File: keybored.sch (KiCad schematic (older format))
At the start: 7 parts, among them U1 ATMEGA32U4

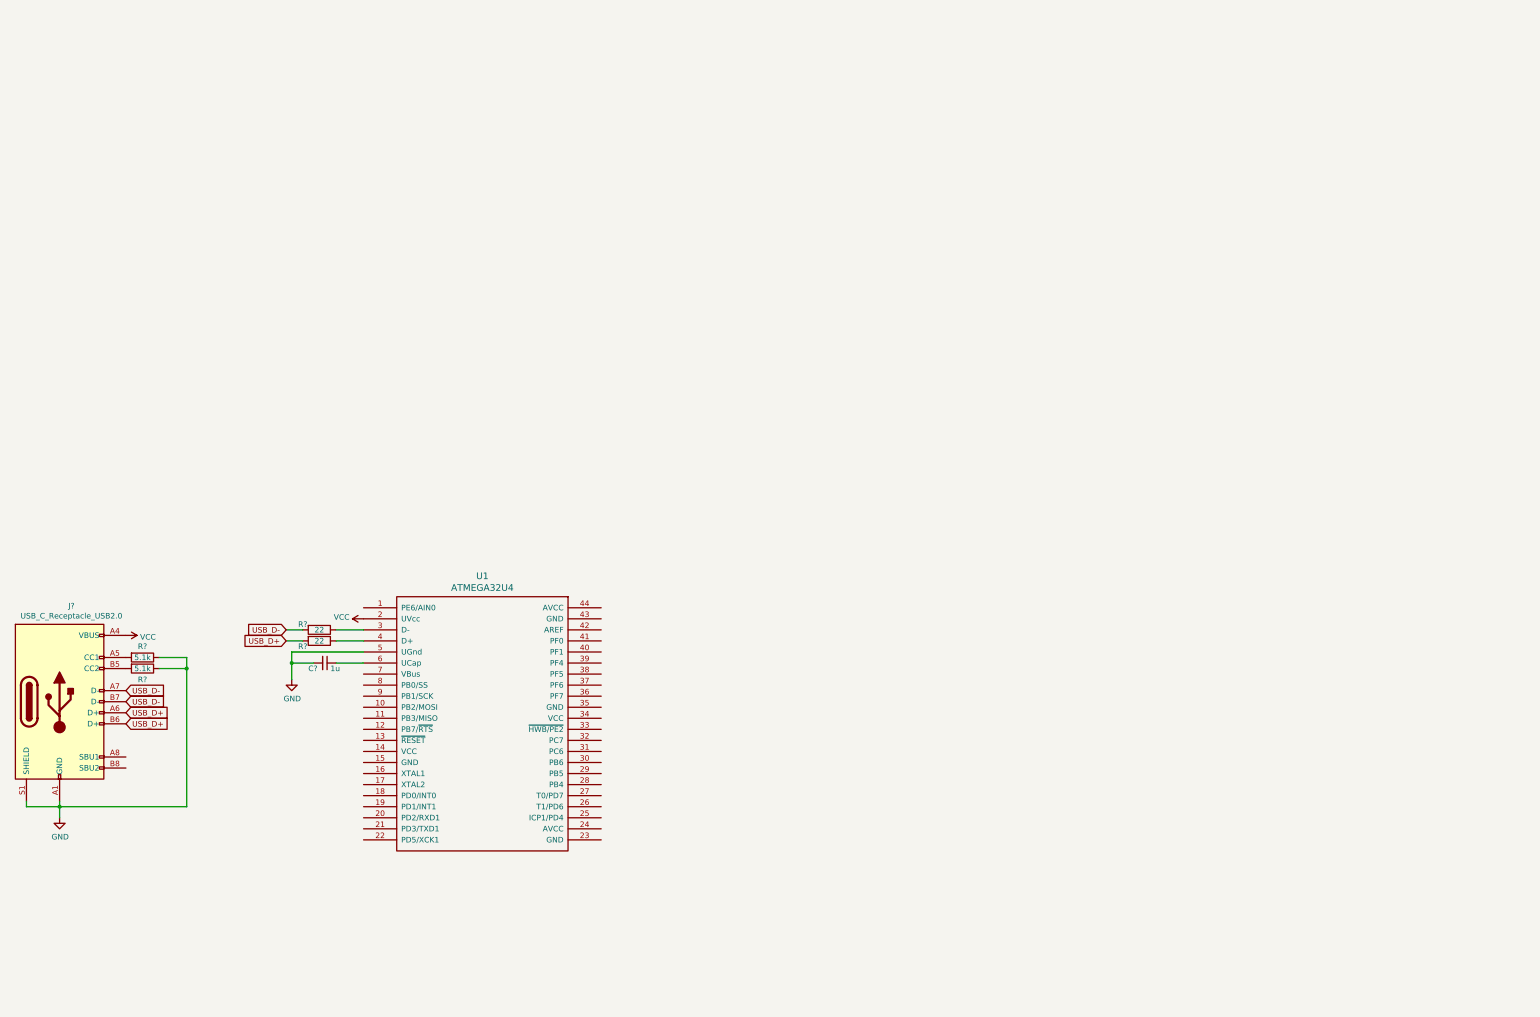
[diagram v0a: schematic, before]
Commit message: Added Schematic
- USB, reset implemented
- matrix pinouts still WIP
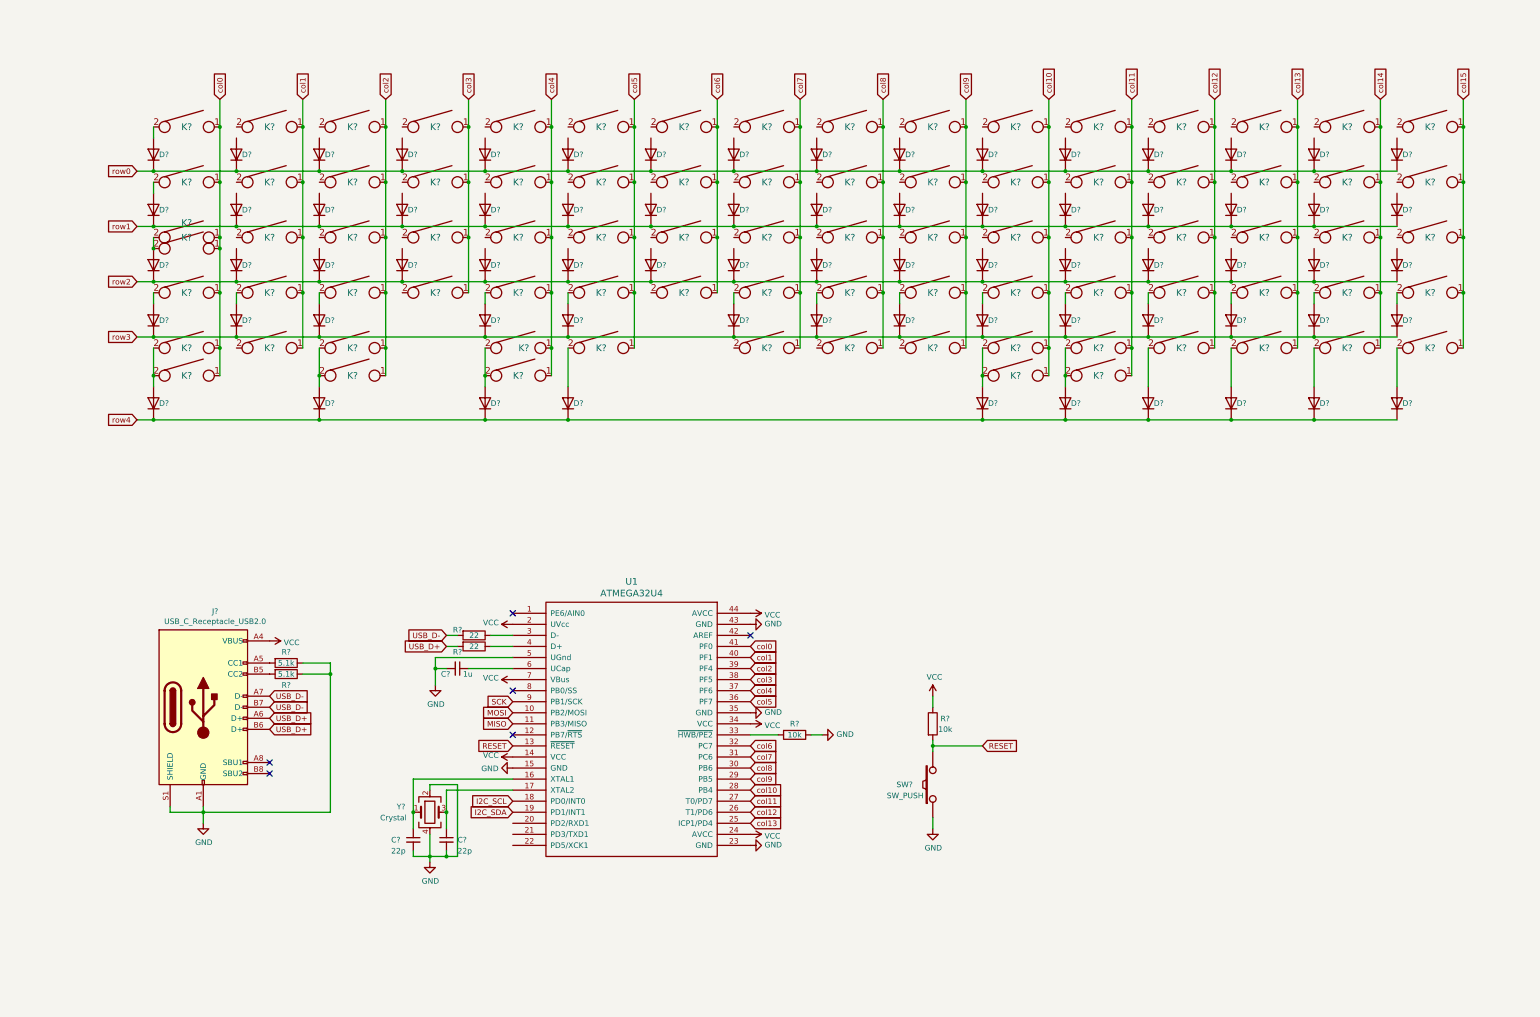
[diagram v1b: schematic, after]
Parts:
- added C? (x2): 22p, symbol Device:C_Small
- added D? (x72): D, symbol Device:D
- added K? (x84): KEYSW, symbol keyboard_parts:KEYSW
- added R? (x2): 10k, symbol Device:R
- added SW?: SW_PUSH, symbol keyboard_parts:SW_PUSH
- added Y?: Crystal, symbol Device:Crystal_GND24
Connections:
- net GND: now also U1.15 (GND), U1.23 (GND), U1.35 (GND), U1.43 (GND), C?.2, C?.2, R?.1, SW?.1, Y?.2, Y?.4
- net VCC: now also U1.14 (VCC), U1.24 (AVCC), U1.34 (VCC), U1.44 (AVCC), U1.7 (VBus), R?.1
- net MOSI: now reaches U1.10 (PB2/MOSI)
- net MISO: now reaches U1.11 (PB3/MISO)
- net RESET: now reaches U1.13 (~RESET)
- net RESET: now also R?.2, SW?.2
- net at U1.16 (XTAL1): now also C?.1, Y?.1
- net at U1.17 (XTAL2): now also C?.1, Y?.3
- net I2C_SCL: now reaches U1.18 (PD0/INT0)
- net I2C_SDA: now reaches U1.19 (PD1/INT1)
- net col13: now reaches U1.25 (ICP1/PD4)
- net col13: now also K?.1, K?.1, K?.1, K?.1, K?.1
- net col12: now reaches U1.26 (T1/PD6)
- net col12: now also K?.1, K?.1, K?.1, K?.1, K?.1
- net col11: now reaches U1.27 (T0/PD7)
- net col11: now also K?.1, K?.1, K?.1, K?.1, K?.1, K?.1
- net col10: now reaches U1.28 (PB4)
- net col10: now also K?.1, K?.1, K?.1, K?.1, K?.1, K?.1
- net col9: now reaches U1.29 (PB5)
- net col9: now also K?.1, K?.1, K?.1, K?.1, K?.1
- net col8: now reaches U1.30 (PB6)
- net col8: now also K?.1, K?.1, K?.1, K?.1, K?.1
- net col7: now reaches U1.31 (PC6)
- net col7: now also K?.1, K?.1, K?.1, K?.1, K?.1
- net col6: now reaches U1.32 (PC7)
- net col6: now also K?.1, K?.1, K?.1, K?.1
- net at U1.33 (~HWB/PE2): now also R?.2
- net col5: now reaches U1.36 (PF7)
- net col5: now also K?.1, K?.1, K?.1, K?.1, K?.1
- net col4: now reaches U1.37 (PF6)
- net col4: now also K?.1, K?.1, K?.1, K?.1, K?.1, K?.1
- net col3: now reaches U1.38 (PF5)
- net col3: now also K?.1, K?.1, K?.1, K?.1
- net col2: now reaches U1.39 (PF4)
- net col2: now also K?.1, K?.1, K?.1, K?.1, K?.1, K?.1
- net col1: now reaches U1.40 (PF1)
- net col1: now also K?.1, K?.1, K?.1, K?.1, K?.1
- net col0: now reaches U1.41 (PF0)
- net col0: now also K?.1, K?.1, K?.1, K?.1, K?.1, K?.1, K?.1
- net SCK: now reaches U1.9 (PB1/SCK)
- new net: D?.2 (A), K?.2 (x21)
- new net: D?.2 (A), K?.2, K?.2 (x6)
- new net col14: K?.1, K?.1, K?.1, K?.1, K?.1
- new net col15: K?.1, K?.1, K?.1, K?.1, K?.1
- new net row0: D?.1 (K), D?.1 (K), D?.1 (K), D?.1 (K), D?.1 (K), D?.1 (K), D?.1 (K), D?.1 (K), D?.1 (K), D?.1 (K), D?.1 (K), D?.1 (K), D?.1 (K), D?.1 (K), D?.1 (K), D?.1 (K)
- new net row1: D?.1 (K), D?.1 (K), D?.1 (K), D?.1 (K), D?.1 (K), D?.1 (K), D?.1 (K), D?.1 (K), D?.1 (K), D?.1 (K), D?.1 (K), D?.1 (K), D?.1 (K), D?.1 (K), D?.1 (K), D?.1 (K)
- new net row2: D?.1 (K), D?.1 (K), D?.1 (K), D?.1 (K), D?.1 (K), D?.1 (K), D?.1 (K), D?.1 (K), D?.1 (K), D?.1 (K), D?.1 (K), D?.1 (K), D?.1 (K), D?.1 (K), D?.1 (K), D?.1 (K)
- new net row3: D?.1 (K), D?.1 (K), D?.1 (K), D?.1 (K), D?.1 (K), D?.1 (K), D?.1 (K), D?.1 (K), D?.1 (K), D?.1 (K), D?.1 (K), D?.1 (K), D?.1 (K), D?.1 (K)
- new net row4: D?.1 (K), D?.1 (K), D?.1 (K), D?.1 (K), D?.1 (K), D?.1 (K), D?.1 (K), D?.1 (K), D?.1 (K), D?.1 (K)
- no-connect marks 0 -> 6
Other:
- moved on the sheet: C?, J?, R?, U1

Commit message: Designations and footprints assigned
- added component references + footprints
- started PCB design
- added rotary encoder and OLED
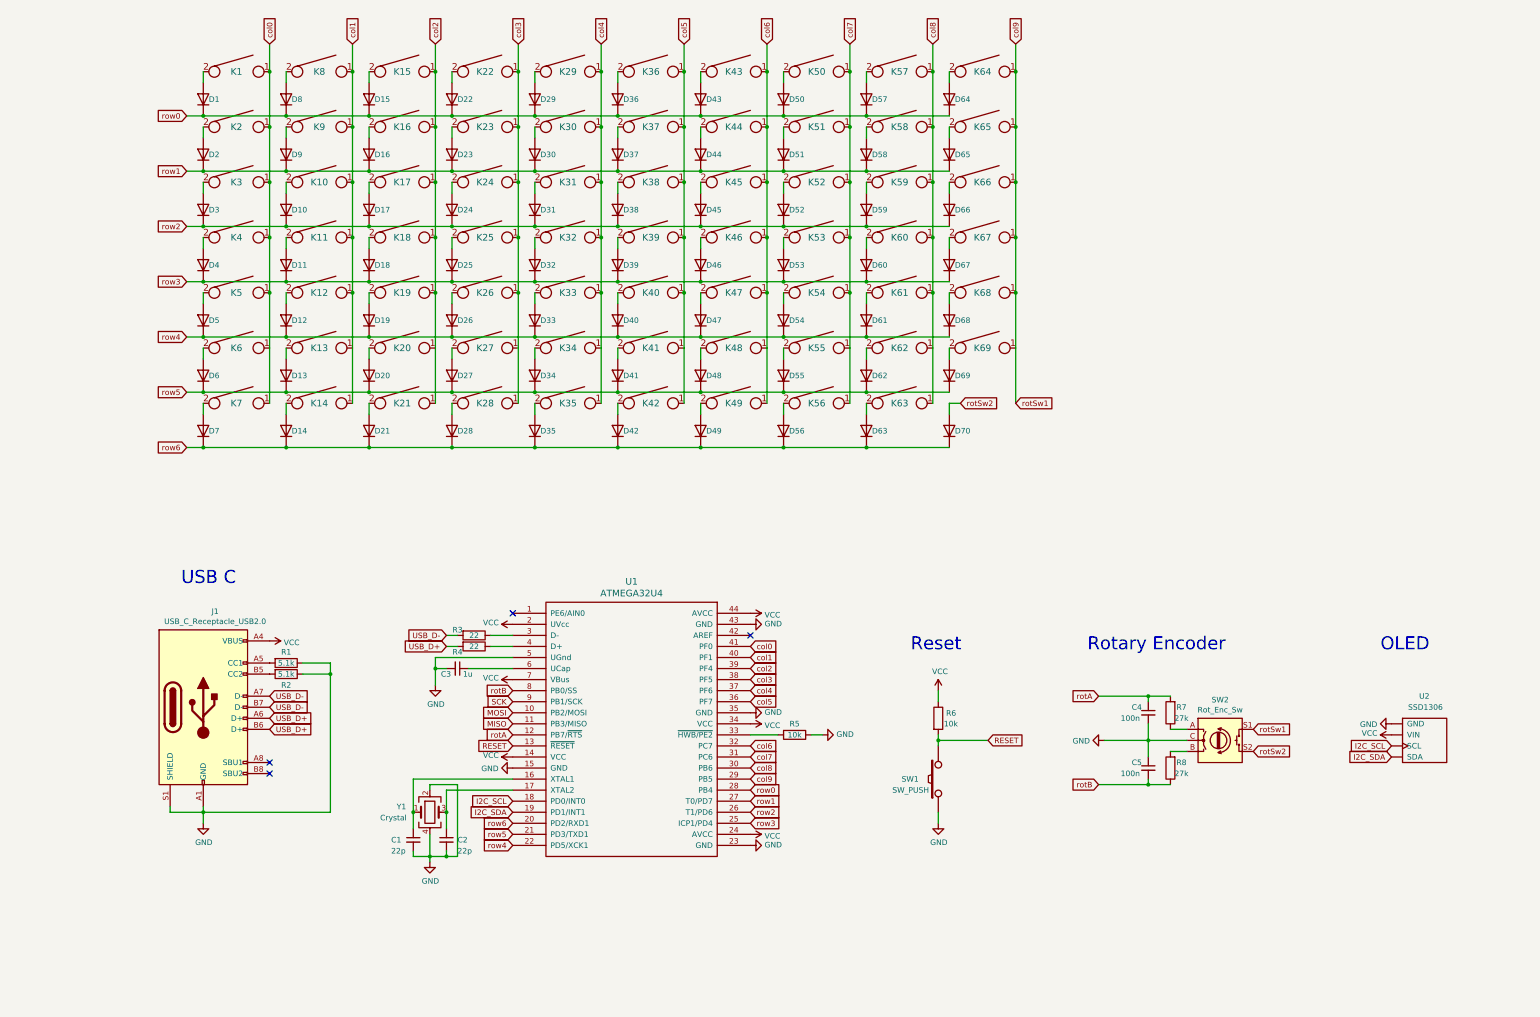
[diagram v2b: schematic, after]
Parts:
- removed D? (x42): D, symbol Device:D
- removed K? (x44): KEYSW, symbol keyboard_parts:KEYSW
- added C4, C5: 100n, keyboard_parts:D_SOD123_axial, symbol Device:C_Small
- added D11, D12, D13, D14, D18, D19, D20, D21, D25, D26, D27, D28, D32, D33, D34, D35, D39, D4, D40, D41, D42, D46, D47, D48, D49, D5, D53, D54, D55, D56, D6, D60, D61, D62, D63, D67, D68, D69, D7, D70: D, keyboard_parts:D_SOD123_axial, symbol Device:D
- added K12, K13, K14, K19, K20, K21, K26, K27, K28, K33, K34, K35, K40, K41, K42, K47, K48, K49, K5, K54, K55, K56, K6, K61, K62, K63, K68, K69, K7: KEYSW, keyswitches:Kailh_socket_PG1350, symbol keyboard_parts:KEYSW
- added R7, R8: 27k, Resistor_SMD:R_0805_2012Metric_Pad1.15x1.40mm_HandSolder, symbol Device:R
- added SW2: Rot_Enc_Sw, Rotary_Encoder:RotaryEncoder_Alps_EC11E-Switch_Vertical_H20mm, symbol Device:Rotary_Encoder_Switch
- added U2: SSD1306, Connector_PinHeader_1.00mm:PinHeader_1x04_P1.00mm_Vertical, symbol Display_Graphic:SSD1306
- C1, C2, C3: renamed from C?; footprint (none) -> keyboard_parts:D_SOD123_axial
- D1, D10, D15, D16, D17, D2, D22, D23, D24, D29, D3, D30, D31, D36, D37, D38, D43, D44, D45, D50, D51, D52, D57, D58, D59, D64, D65, D66, D8, D9: renamed from D?; footprint (none) -> keyboard_parts:D_SOD123_axial
- J1: renamed from J?; footprint (none) -> Type-C:USB_C_GCT_USB4085
- K1, K10, K11, K15, K16, K17, K18, K2, K22, K23, K24, K25, K29, K3, K30, K31, K32, K36, K37, K38, K39, K4, K43, K44, K45, K46, K50, K51, K52, K53, K57, K58, K59, K60, K64, K65, K66, K67, K8, K9: renamed from K?; footprint (none) -> keyswitches:Kailh_socket_PG1350
- R1, R2, R3, R4, R5, R6: renamed from R?; footprint (none) -> Resistor_SMD:R_0805_2012Metric_Pad1.15x1.40mm_HandSolder
- SW1: renamed from SW?; footprint (none) -> Button_Switch_SMD:SW_SPST_TL3342
- U1: footprint (none) -> Package_QFP:TQFP-44_10x10mm_P0.8mm
- Y1: renamed from Y?; footprint (none) -> Crystal:Crystal_SMD_SeikoEpson_FA238-4Pin_3.2x2.5mm_HandSoldering
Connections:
- net col10 is gone; now on net row0: U1.28 (PB4)
- net col11 is gone; now on net row1: U1.27 (T0/PD7)
- net col12 is gone; now on net row2: U1.26 (T1/PD6)
- net col13 is gone; now on net row3: U1.25 (ICP1/PD4)
- net GND: now also C4.2, C5.1, SW2.C, U2.~ (VIN)
- net I2C_SCL: now also U2.~ (VIN)
- net I2C_SDA: now also U2.~ (VIN)
- net VCC: now also U2.~ (VIN)
- net col0: now also K5.1, K6.1, K7.1
- net col1: now also K12.1, K13.1, K14.1
- net col2: now also K19.1, K20.1, K21.1
- net col3: now also K26.1, K27.1, K28.1
- net col4: now also K33.1, K34.1, K35.1
- net col5: now also K40.1, K41.1, K42.1
- net col6: now also K47.1, K48.1, K49.1
- net col7: now also K54.1, K55.1, K56.1
- net col8: now also K61.1, K62.1, K63.1
- net col9: now also K68.1, K69.1, SW2.S1
- net row3: now also D11.1 (K), D18.1 (K), D25.1 (K), D32.1 (K), D39.1 (K), D4.1 (K), D46.1 (K), D53.1 (K), D60.1 (K), D67.1 (K)
- net row4: now also U1.22 (PD5/XCK1), D12.1 (K), D19.1 (K), D26.1 (K), D33.1 (K), D40.1 (K), D47.1 (K), D5.1 (K), D54.1 (K), D61.1 (K), D68.1 (K)
- net rotA: now reaches U1.12 (PB7/~RTS)
- net rotA: now also C4.1, R7.2
- net row6: now reaches U1.20 (PD2/RXD1)
- net row6: now also D14.1 (K), D21.1 (K), D28.1 (K), D35.1 (K), D42.1 (K), D49.1 (K), D56.1 (K), D63.1 (K), D7.1 (K), D70.1 (K)
- net row5: now reaches U1.21 (PD3/TXD1)
- net row5: now also D13.1 (K), D20.1 (K), D27.1 (K), D34.1 (K), D41.1 (K), D48.1 (K), D55.1 (K), D6.1 (K), D62.1 (K), D69.1 (K)
- net rotB: now reaches U1.8 (PB0/SS)
- net rotB: now also C5.2, R8.1
- net at K8.2: now also D8.2 (A)
- net at K22.2: now also D22.2 (A)
- net at K15.2: now also D15.2 (A)
- net at K29.2: now also D29.2 (A)
- net at K43.2: now also D43.2 (A)
- net at K36.2: now also D36.2 (A)
- net at K57.2: now also D57.2 (A)
- net at K50.2: now also D50.2 (A)
- net at K64.2: now also D64.2 (A)
- net at K9.2: now also D9.2 (A)
- net at K23.2: now also D23.2 (A)
- net at K16.2: now also D16.2 (A)
- net at K30.2: now also D30.2 (A)
- net at K44.2: now also D44.2 (A)
- net at K37.2: now also D37.2 (A)
- net at K58.2: now also D58.2 (A)
- net at K51.2: now also D51.2 (A)
- net at K65.2: now also D65.2 (A)
- net at K10.2: now also D10.2 (A)
- net at K24.2: now also D24.2 (A)
- net at K17.2: now also D17.2 (A)
- net at K31.2: now also D31.2 (A)
- net at K45.2: now also D45.2 (A)
- net at K38.2: now also D38.2 (A)
- net at K59.2: now also D59.2 (A)
- net at K52.2: now also D52.2 (A)
- net at K66.2: now also D66.2 (A)
- net at K11.2: now also D11.2 (A)
- net at K4.2: now also D4.2 (A)
- net at K25.2: now also D25.2 (A)
- net at K18.2: now also D18.2 (A)
- net at K32.2: now also D32.2 (A)
- net at K46.2: now also D46.2 (A)
- net at K39.2: now also D39.2 (A)
- net at K60.2: now also D60.2 (A)
- net at K53.2: now also D53.2 (A)
- net at K67.2: now also D67.2 (A)
- new net: D69.2 (A), K69.2
- new net: D62.2 (A), K62.2
- new net: D55.2 (A), K55.2
- new net: D48.2 (A), K48.2
- new net: D41.2 (A), K41.2
- new net: D34.2 (A), K34.2
- new net: D27.2 (A), K27.2
- new net: D20.2 (A), K20.2
- new net: D13.2 (A), K13.2
- new net: D6.2 (A), K6.2
- new net: D35.2 (A), K35.2
- new net: D56.2 (A), K56.2
- new net: D63.2 (A), K63.2
- new net: D42.2 (A), K42.2
- new net: D49.2 (A), K49.2
- new net: D21.2 (A), K21.2
- new net: D28.2 (A), K28.2
- new net: D7.2 (A), K7.2
- new net: D14.2 (A), K14.2
- new net: R7.1, SW2.A
- new net: R8.2, SW2.B
- new net: D12.2 (A), K12.2
- new net: D5.2 (A), K5.2
- new net: D26.2 (A), K26.2
- new net: D19.2 (A), K19.2
- new net: D33.2 (A), K33.2
- new net: D47.2 (A), K47.2
- new net: D40.2 (A), K40.2
- new net: D61.2 (A), K61.2
- new net: D54.2 (A), K54.2
- new net: D68.2 (A), K68.2
- new net rotSw2: D70.2 (A), SW2.S2
- no-connect marks 6 -> 4
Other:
- note added: "OLED"
- note added: "Reset"
- note added: "Rotary Encoder"
- note added: "USB C"
- moved on the sheet: D1, D10, D15, D16, D17, D2, D22, D23, D24, D29, D3, D30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

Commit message: Diode layout and row routing
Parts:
- C1, C2, C3, C4, C5: footprint keyboard_parts:D_SOD123_axial -> Capacitor_SMD:C_0805_2012Metric_Pad1.15x1.40mm_HandSolder
- D1, D10, D11, D12, D13, D14, D15, D16, D17, D18, D19, D2, D20, D21, D22, D23, D24, D25, D26, D27, D28, D29, D3, D30, D31, D32, D33, D34, D35, D36, D37, D38, D39, D4, D40, D41, D42, D43, D44, D45, D46, D47, D48, D49, D5, D50, D51, D52, D53, D54, D55, D56, D57, D58, D59, D6, D60, D61, D62, D63, D64, D65, D66, D67, D68, D69, D7, D70, D8, D9: footprint keyboard_parts:D_SOD123_axial -> keybored:DO-35_SOD27_5.08mm
- K1, K10, K11, K12, K13, K14, K15, K16, K17, K18, K19, K2, K20, K21, K22, K23, K24, K25, K26, K27, K28, K29, K3, K30, K31, K32, K33, K34, K35, K36, K37, K38, K39, K4, K40, K41, K42, K43, K44, K45, K46, K47, K48, K49, K5, K50, K51, K52, K53, K54, K55, K56, K57, K58, K59, K6, K60, K61, K62, K63, K64, K65, K66, K67, K68, K69, K7, K8, K9: footprint keyswitches:Kailh_socket_PG1350 -> keyswitches:Kailh_socket_MX
- U2: symbol Display_Graphic:SSD1306 -> keybored-rescue:SSD1306-Display_Graphic
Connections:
- net GND: now also U2.1 (GND); no longer U2.~ (VIN)
- net I2C_SCL: now also U2.3 (SCL); no longer U2.~ (VIN)
- net I2C_SDA: now also U2.4 (SDA); no longer U2.~ (VIN)
- net VCC: now also U2.2 (VIN); no longer U2.~ (VIN)

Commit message: Finished PCB routing rev 1
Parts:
- removed D42, D55, D56: D, keybored:DO-35_SOD27_5.08mm, symbol Device:D
- removed K42, K55, K56: KEYSW, keyswitches:Kailh_socket_MX, symbol keyboard_parts:KEYSW
- added C10, C11, C6, C7, C8, C9: 0.1u, Capacitor_SMD:C_0805_2012Metric_Pad1.15x1.40mm_HandSolder, symbol Device:C_Small
- added C13: 4.7u, Capacitor_SMD:C_0805_2012Metric_Pad1.15x1.40mm_HandSolder, symbol Device:C_Small
- added R10, R9: 4.7k, Resistor_SMD:R_0805_2012Metric_Pad1.15x1.40mm_HandSolder, symbol Device:R
- U2: value SSD1306 -> SSD1306-Display_Graphic; footprint Connector_PinHeader_1.00mm:PinHeader_1x04_P1.00mm_Vertical -> keybored:SSD1306_OLED_128x32_0.91_inch
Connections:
- net GND: now also C10.2, C11.2, C13.2, C6.2, C7.2, C8.2, C9.2
- net I2C_SCL: now also R10.1
- net I2C_SDA: now also R9.1
- net VCC: now also C10.1, C11.1, C13.1, C6.1, C7.1, C8.1, C9.1, R10.2, R9.2
